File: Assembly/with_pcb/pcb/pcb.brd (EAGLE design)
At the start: 227.5 x 77.2 mm, 213 parts, among them J1 USB-TYPE-C", U2 M2.5-HOLE, U3 M2.5-HOLE, U4 M2.5-HOLE, U5 M2.5-HOLE, U6 M2.5-HOLE, U7 M2.5-HOLE, U8 M2.5-HOLE

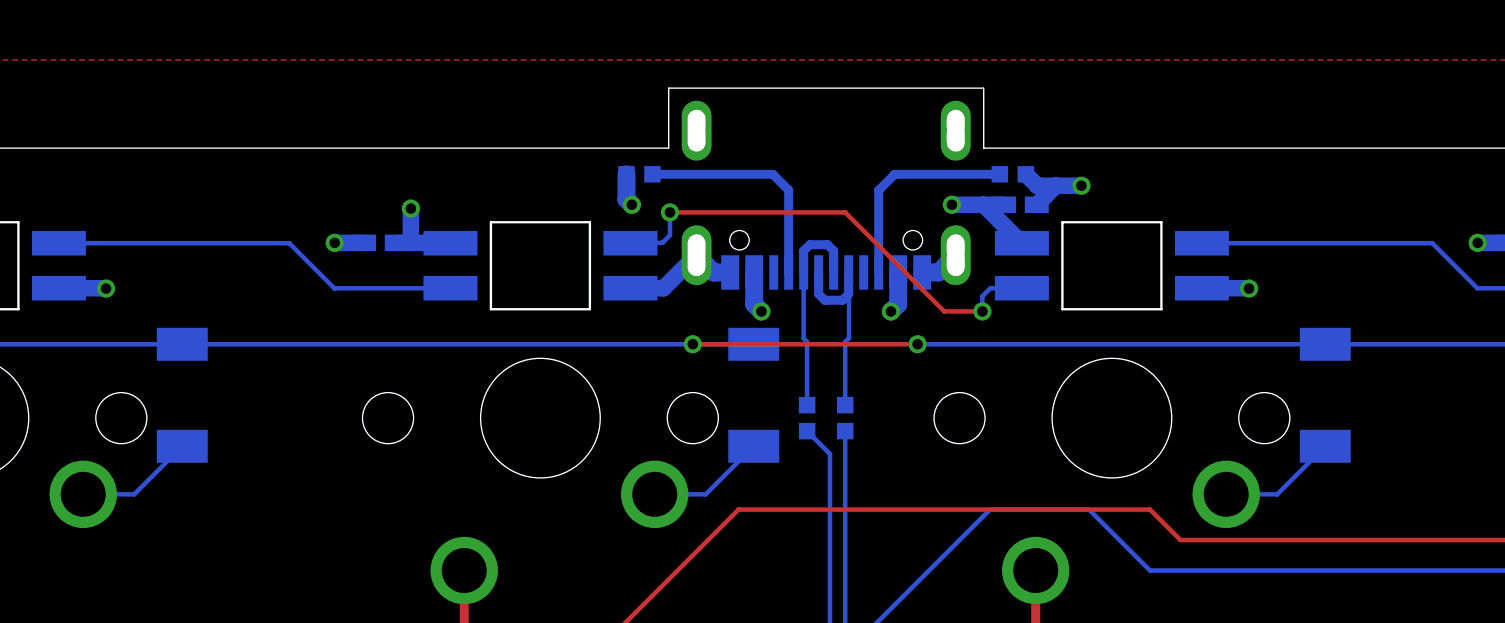
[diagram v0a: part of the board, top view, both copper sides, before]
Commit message: Gave more space for connection between ground plane and USB connection
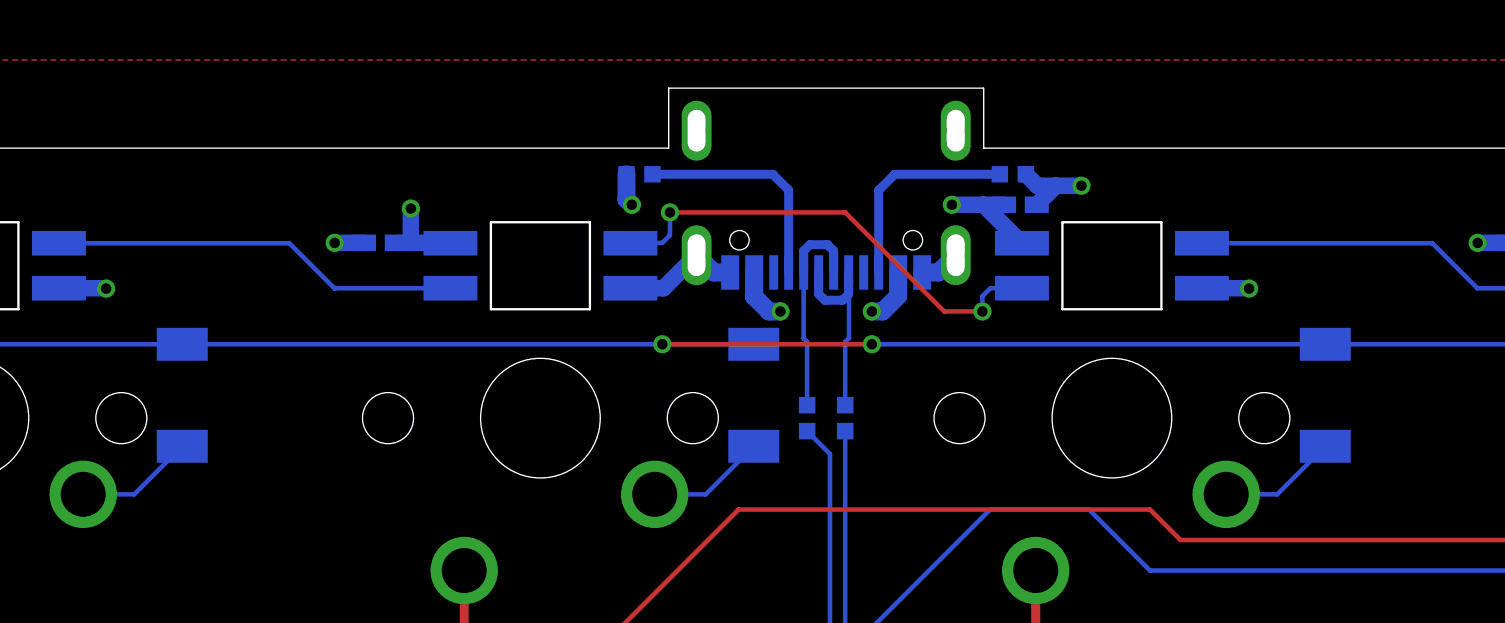
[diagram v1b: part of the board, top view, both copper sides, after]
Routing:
- net ROW_A: track 291.7 -> 292.7 mm
- net +5V: track 158.2 -> 159.1 mm
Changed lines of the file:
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@@
 <grid distance="0.508" unitdist="mm" unit="mm" style="lines" multiple="1" display="yes" altdistance="5" altunitdist="mil" altunit="mil"/>
 <layers>
-<layer number="1" name="Top" color="4" fill="1" visible="yes" active="yes"/>
+<layer number="1" name="Top" color="4" fill="1" visible="no" active="yes"/>
 <layer number="2" name="Route2" color="16" fill="1" visible="no" active="yes"/>
 <layer number="3" name="Route3" color="17" fill="1" visible="no" active="no"/>
@@
 <layer number="13" name="Route13" color="21" fill="1" visible="no" active="no"/>
 <layer number="14" name="Route14" color="22" fill="1" visible="no" active="no"/>
-<layer number="15" name="Route15" color="23" fill="1" visible="no" active="yes"/>
+<layer number="15" name="Route15" color="23" fill="1" visible="yes" active="yes"/>
 <layer number="16" name="Bottom" color="1" fill="1" visible="yes" active="yes"/>
 <layer number="17" name="Pads" color="2" fill="1" visible="yes" active="yes"/>
@@
 <wire x1="35.1" y1="82.042" x2="35.1" y2="82.03" width="0.55" layer="16"/>
 <via x="33.782" y="83.185" extent="1-16" drill="0.35"/>
-<wire x1="45.225" y1="81.056" x2="45.225" y2="79.997" width="0.6" layer="16"/>
-<wire x1="45.225" y1="79.997" x2="45.466" y2="79.756" width="0.6" layer="16"/>
-<via x="45.466" y="79.756" extent="1-16" drill="0.35"/>
-<wire x1="50.025" y1="81.056" x2="50.025" y2="79.997" width="0.6" layer="16"/>
-<wire x1="50.025" y1="79.997" x2="49.784" y2="79.756" width="0.6" layer="16"/>
-<via x="49.784" y="79.756" extent="1-16" drill="0.35"/>
+<via x="46.101" y="79.756" extent="1-16" drill="0.35"/>
+<via x="49.149" y="79.756" extent="1-16" drill="0.35"/>
 <via x="51.816" y="83.312" extent="1-16" drill="0.35"/>
 <wire x1="73.188" y1="82.042" x2="73.2" y2="82.03" width="0.6" layer="16"/>
@@
 <wire x1="52.32191875" y1="42.16191875" x2="51.81808125" y2="42.16191875" width="0.3" layer="16"/>
 <wire x1="52.578" y1="42.418" x2="52.32191875" y2="42.16191875" width="0.3" layer="16"/>
+<wire x1="45.225" y1="80.27389375" x2="45.213553125" y2="80.262446875" width="0.6" layer="16"/>
+<wire x1="45.225" y1="81.056" x2="45.225" y2="80.27389375" width="0.6" layer="16"/>
+<wire x1="45.213553125" y1="80.262446875" x2="45.72" y2="79.756" width="0.6" layer="16"/>
+<wire x1="45.72" y1="79.756" x2="46.101" y2="79.756" width="0.6" layer="16"/>
+<wire x1="50.025" y1="81.056" x2="50.025" y2="80.27389375" width="0.6" layer="16"/>
+<wire x1="49.50710625" y1="79.756" x2="49.149" y2="79.756" width="0.6" layer="16"/>
+<wire x1="50.025" y1="80.27389375" x2="49.50710625" y2="79.756" width="0.6" layer="16"/>
 </signal>
 <signal name="N$9">
@@
 <contactref element="D11" pad="P$1"/>
 <contactref element="U1" pad="P$39"/>
-<via x="43.18" y="78.662" extent="1-16" drill="0.35"/>
-<via x="50.673" y="78.662" extent="1-16" drill="0.35"/>
+<via x="42.164" y="78.662" extent="1-16" drill="0.35"/>
+<via x="49.149" y="78.662" extent="1-16" drill="0.35"/>
 <wire x1="64.213" y1="78.613" x2="64.262" y2="78.662" width="0.3" layer="16"/>
 <wire x1="64.164" y1="78.662" x2="64.213" y2="78.613" width="0.3" layer="16"/>
@@
 <wire x1="11.176" y1="48.641" x2="12.192" y2="47.625" width="0.1524" layer="16"/>
 <wire x1="12.114" y1="78.662" x2="26.162" y2="78.662" width="0.1524" layer="16"/>
-<wire x1="26.162" y1="78.662" x2="43.18" y2="78.662" width="0.1524" layer="16"/>
-<wire x1="43.18" y1="78.662" x2="45.212" y2="78.662" width="0.1524" layer="16"/>
-<wire x1="50.673" y1="78.662" x2="64.164" y2="78.662" width="0.1524" layer="16"/>
+<wire x1="26.162" y1="78.662" x2="42.164" y2="78.662" width="0.1524" layer="16"/>
+<wire x1="42.164" y1="78.662" x2="45.212" y2="78.662" width="0.1524" layer="16"/>
+<wire x1="49.149" y1="78.662" x2="64.164" y2="78.662" width="0.1524" layer="16"/>
 <wire x1="64.262" y1="78.662" x2="83.312" y2="78.662" width="0.1524" layer="16"/>
 <wire x1="83.312" y1="78.662" x2="102.362" y2="78.662" width="0.1524" layer="16"/>
@@
 <wire x1="197.612" y1="78.662" x2="216.662" y2="78.662" width="0.1524" layer="16"/>
 <wire x1="216.662" y1="78.662" x2="235.839" y2="78.662" width="0.1524" layer="16"/>
-<wire x1="43.18" y1="78.662" x2="50.673" y2="78.662" width="0.1524" layer="1"/>
+<wire x1="42.164" y1="78.662" x2="49.149" y2="78.662" width="0.1524" layer="1"/>
 </signal>
 <signal name="COL_12">
